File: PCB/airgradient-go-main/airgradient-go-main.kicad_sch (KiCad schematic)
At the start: 205 parts, among them CN1 HCZZ0032-5, CN2 HCZZ0032-5, CN3 HCZZ0032-5, Q1 SIA445EDJ-T1-GE3, Q2 ZVN4106FTA_C508255, Q3 CSD83325L, Q4 SS8050-G, Q5 SI1308EDL, SW1 TS-1091C-A1B3-D2, SW2 TS-1091C-A1B3-D2, U1 W25N512GVEIG, U10 SGP41-D-R4, U11 PS1-CO-SMOKE-10k, U12 SHT4x, U13 SPL07-003, U14 LIS2DH12TR, U15 TMUX121NKGR_C22428404, U16 S12, U17 TCA6408ARGT, U18 TAU1113, U19 LM66200DRLR, U2 ZDSD512MLGEAG, U20 LP5036, U3 BQ27742YZFR-G1, U4 ESP32-C5-MINI-1, U5 BQ25628RYKR, U6 HYG-8503A, U7 TPL5010DDCR, U8 TPS63802DLAR, U9 TPS7A0228DQNR, Y1 32.768kHz CL6pF

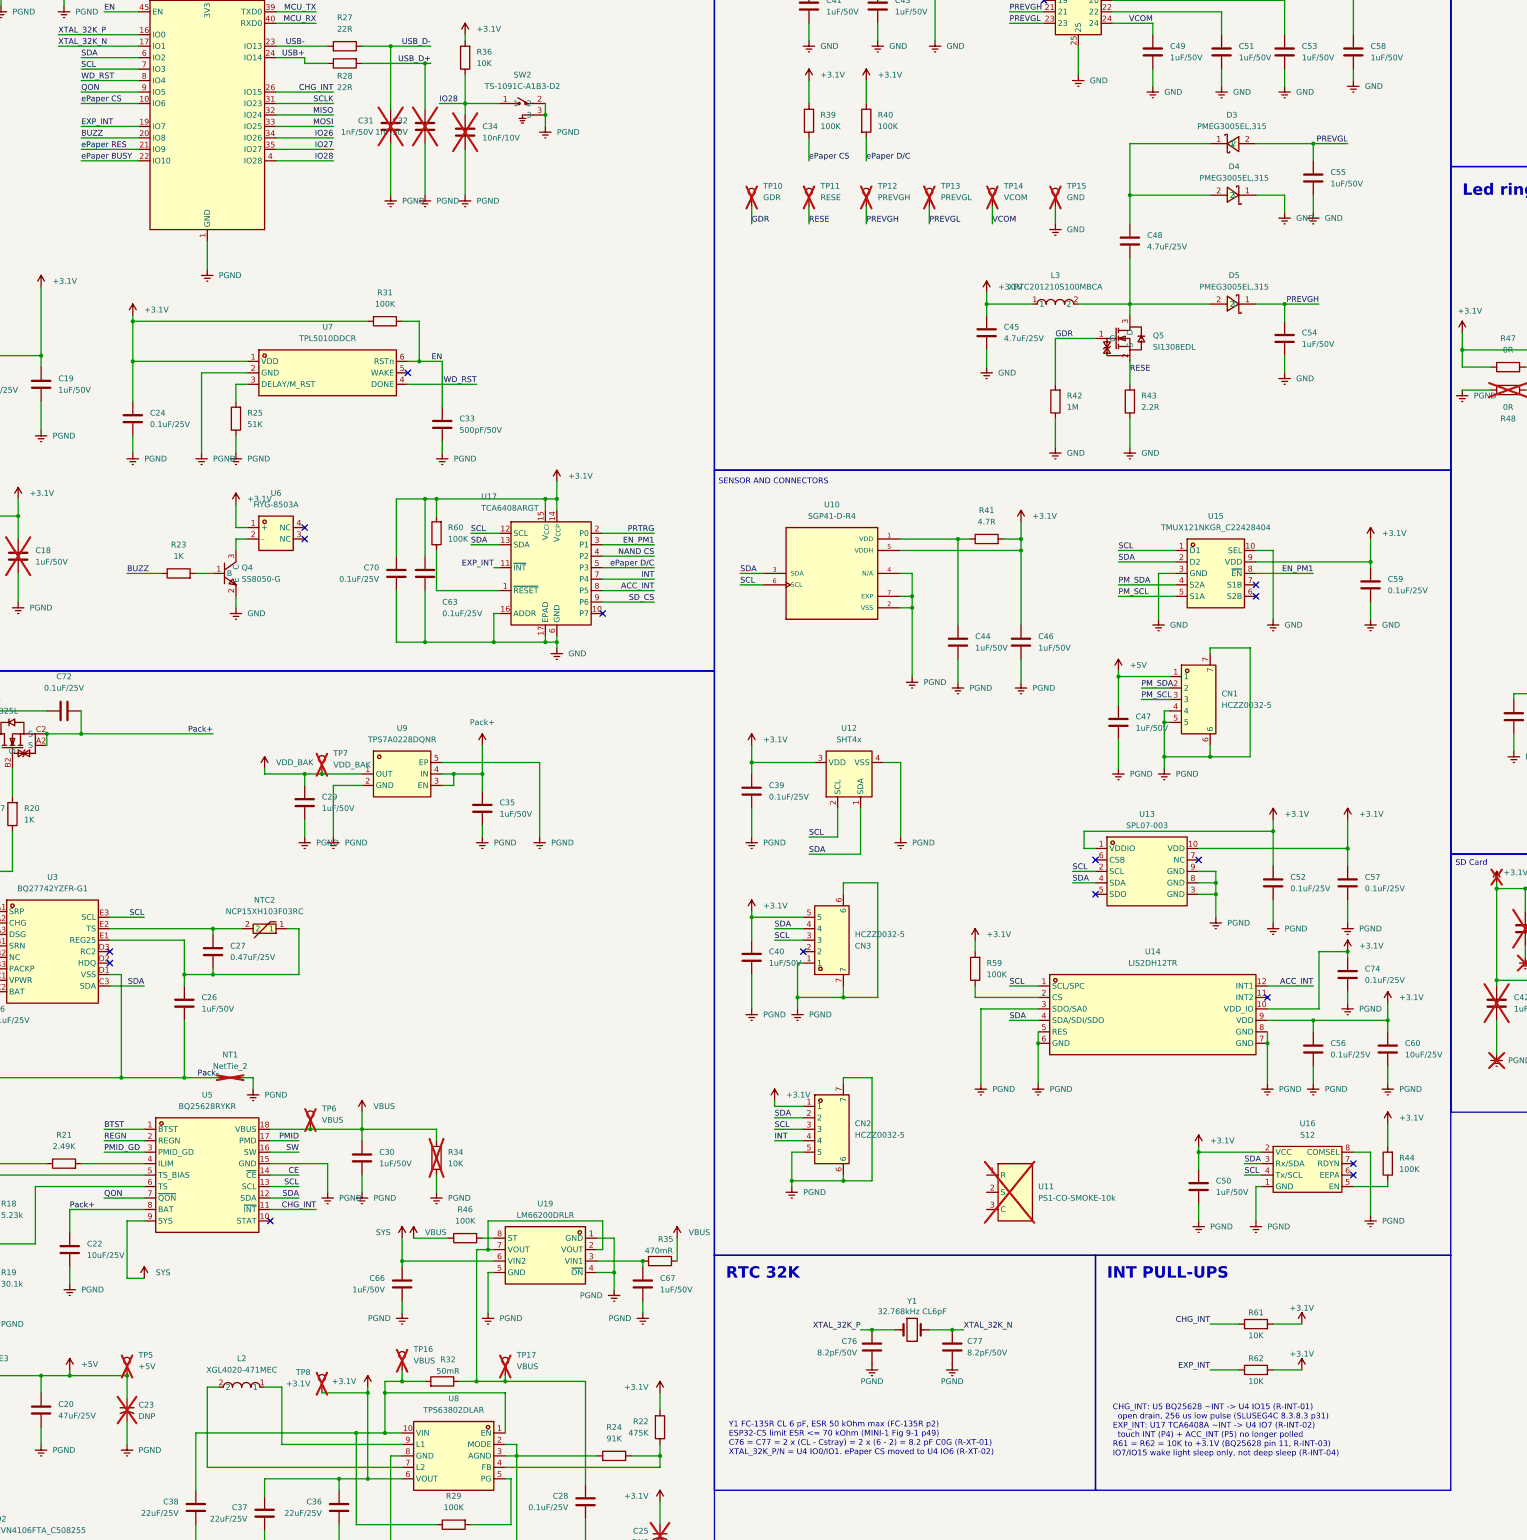
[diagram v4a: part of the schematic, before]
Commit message: Wire-OR the charger and expander INT onto IO7
At layout, U5 pin 11, U17 pin 11 and the IO15 pad turned out to be
walled in by existing routing (SDA escape via and SYS pour at U5,
SCL/SD_CS at U17, UART/NAND CS/MOSI at IO15). Both INT outputs are
open drain, so they now share one net, I2C_INT, into U4 IO7 with a
single 10K pull-up (R61); R62 is gone and IO15 is free again.

Firmware reads the TCA6408A input port and Charger_Flag_X on every
falling edge; the charger flags latch, so a pulse that arrives while
the expander holds the line low is not lost (R-INT-01..04).

lint: no new findings; ERC 269 -> 268 vs 1d977c7; net_diff 0 errors.
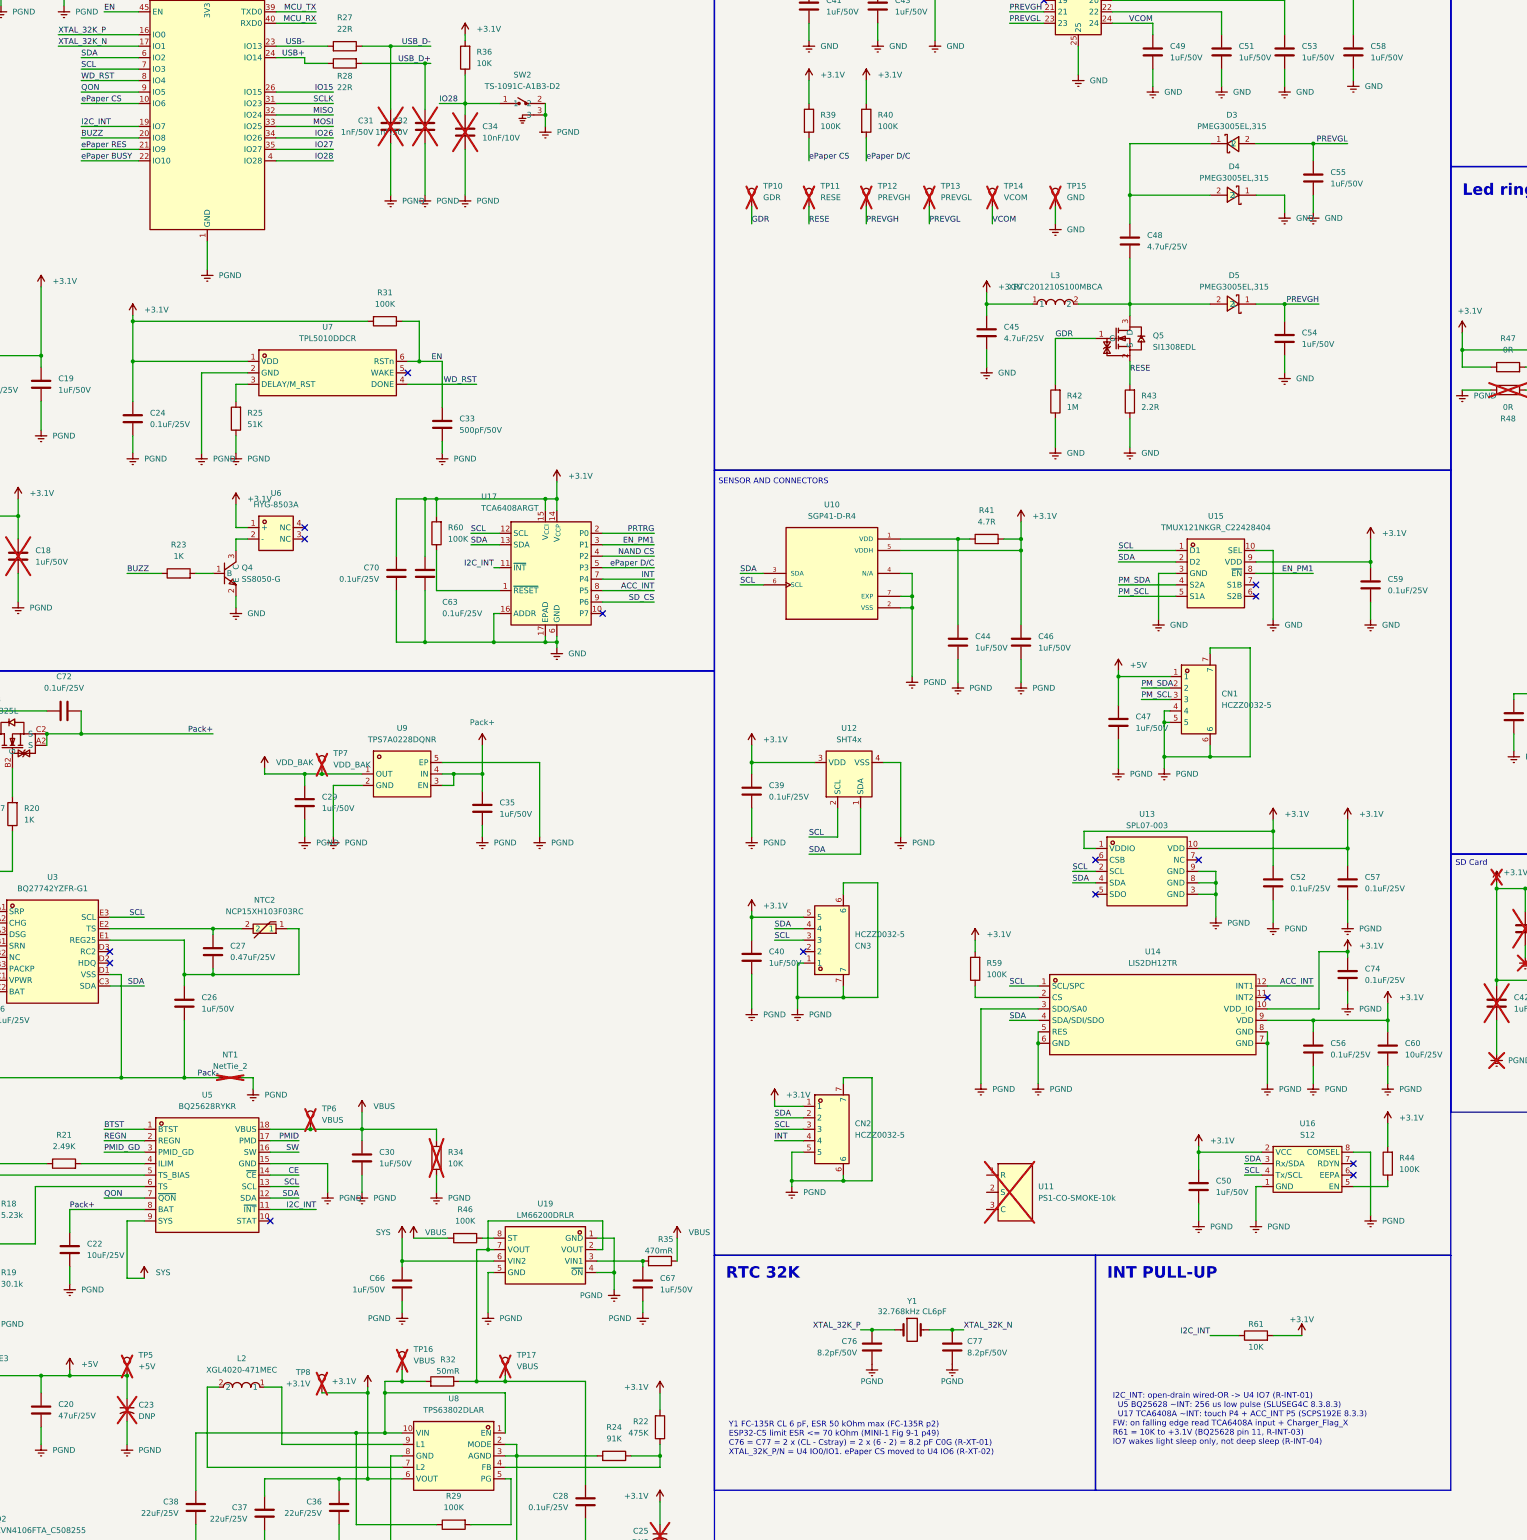
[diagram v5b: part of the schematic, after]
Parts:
- removed R62: 10K, Resistor_SMD:R_0402_1005Metric, symbol Device:R
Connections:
- net EXP_INT is gone; now on net I2C_INT: U17.11 (~{INT}), U4.19 (IO7)
- net CHG_INT renamed I2C_INT
- net I2C_INT: no longer U4.26 (IO15)
- new net IO15: U4.26 (IO15)
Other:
- note added: "I2C_INT: open-drain wired-OR -> U4 IO7 (R-INT-01) U5 BQ25628 ~INT: 256 us low pulse (SLUSEG4C 8.3.8.3) U17 TCA6408A ~INT: touch P4 + ACC_INT P5 (SCPS192E 8.3.3) FW: on falling edge read TCA6408A input + Charger_Flag_X R61 = 10K to +3.1V (BQ25628 pin 11, R-INT-03) IO7 wakes light sleep only, not deep sleep (R-INT-04)"
- note added: "INT PULL-UP"
- note removed: "CHG_INT: U5 BQ25628 ~INT -> U4 IO15 (R-INT-01) open drain, 256 us low pulse (SLUSEG4C 8.3.8.3 p31) EXP_INT: U17 TCA6408A ~INT -> U4 IO7 (R-INT-02) touch INT (P4) + ACC_INT (P5) no longer polled R61 = R62 = 10K to +3.1V (BQ25628 pin 11, R-INT-03) IO7/IO15 wake light sleep only, not deep sleep (R-INT-04)"
- note removed: "INT PULL-UPS"
- moved on the sheet: R61
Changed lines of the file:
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@@
 		)
 	)
-	(label "CHG_INT"
+	(label "I2C_INT"
 		(at 172.72 323.85 180)
 		(effects
@@
 		)
 	)
-	(label "EXP_INT"
+	(label "I2C_INT"
 		(at 212.09 181.61 180)
 		(effects
@@
 		)
 	)
-	(label "EXP_INT"
+	(label "I2C_INT"
 		(at 120.65 83.82 0)
 		(effects
@@
 		)
 	)
-	(label "CHG_INT"
+	(label "IO15"
 		(at 176.53 76.2 180)
 		(effects
@@
 	(wire
 		(pts
-			(xy 377.19 349.25) (xy 370.84 349.25)
+			(xy 377.19 351.79) (xy 370.84 351.79)
 		)
 		(stroke
@@
 		)
 	)
-	(label "CHG_INT"
-		(at 370.84 349.25 180)
+	(label "I2C_INT"
+		(at 370.84 351.79 180)
 		(effects
 			(font
@@
 	(wire
 		(pts
-			(xy 384.81 349.25) (xy 391.16 349.25)
-		)
-		(stroke
-			(width 0)
-			(type default)
-		)
-	)
-	(wire
-		(pts
-			(xy 377.19 359.41) (xy 370.84 359.41)
-		)
-		(stroke
-			(width 0)
-			(type default)
-		)
-	)
-	(label "EXP_INT"
-		(at 370.84 359.41 180)
-		(effects
-			(font
-				(size 1.27 1.27)
-			)
-			(justify right bottom)
-		)
-	)
-	(wire
-		(pts
-			(xy 384.81 359.41) (xy 391.16 359.41)
+			(xy 384.81 351.79) (xy 391.16 351.79)
 		)
 		(stroke
@@
 	(symbol
 		(lib_id "Device:R")
-		(at 381 349.25 90)
+		(at 381 351.79 90)
 		(unit 1)
 		(body_style 1)
@@
 		(fields_autoplaced yes)
 		(property "Reference" "R61"
-			(at 381 346.71 90)
+			(at 381 349.25 90)
 			(show_name no)
 			(do_not_autoplace no)
@@
 		)
 		(property "Value" "10K"
-			(at 381 351.79 90)
+			(at 381 354.33 90)
 			(show_name no)
 			(do_not_autoplace no)
@@
 		)
 		(property "Footprint" "Resistor_SMD:R_0402_1005Metric"
-			(at 381 349.25 0)
+			(at 381 351.79 0)
 			(hide yes)
 			(show_name no)
@@
 		)
 		(property "Datasheet" "https://lcsc.com/product-detail/Others_Huaxin-S-T-MR04X1002FTL_C327797.html"
-			(at 381 349.25 0)
+			(at 381 351.79 0)
 			(hide yes)
 			(show_name no)
@@
 		)
 		(property "Description" "MR04X1002FTL"
-			(at 381 349.25 0)
+			(at 381 351.79 0)
 			(hide yes)
 			(show_name no)
@@
 		)
 		(property "LCSC Part" "C327797"
-			(at 381 349.25 0)
+			(at 381 351.79 0)
 			(hide yes)
 			(show_name no)
@@
 	)
 	(symbol
-		(lib_id "Device:R")
-		(at 381 359.41 90)
-		(unit 1)
-		(body_style 1)
-		(exclude_from_sim no)
-		(in_bom yes)
-		(on_board yes)
-		(in_pos_files yes)
-		(dnp no)
-		(fields_autoplaced yes)
-		(property "Reference" "R62"
-			(at 381 356.87 90)
-			(show_name no)
-			(do_not_autoplace no)
-			(effects
-				(font
-					(size 1.27 1.27)
-				)
-			)
-		)
-		(property "Value" "10K"
-			(at 381 361.95 90)
-			(show_name no)
-			(do_not_autoplace no)
-			(effects
-				(font
-					(size 1.27 1.27)
-				)
-			)
-		)
-		(property "Footprint" "Resistor_SMD:R_0402_1005Metric"
-			(at 381 359.41 0)
-			(hide yes)
-			(show_name no)
-			(do_not_autoplace no)
-			(effects
-				(font
-					(size 1.27 1.27)
-				)
-			)
-		)
-		(property "Datasheet" "https://lcsc.com/product-detail/Others_Huaxin-S-T-MR04X1002FTL_C327797.html"
-			(at 381 359.41 0)
-			(hide yes)
-			(show_name no)
-			(do_not_autoplace no)
-			(effects
-				(font
-					(size 1.27 1.27)
-				)
-			)
-		)
-		(property "Description" "MR04X1002FTL"
-			(at 381 359.41 0)
-			(hide yes)
-			(show_name no)
-			(do_not_autoplace no)
-			(effects
-				(font
-					(size 1.27 1.27)
-				)
-			)
-		)
-		(property "LCSC Part" "C327797"
-			(at 381 359.41 0)
-			(hide yes)
-			(show_name no)
-			(do_not_autoplace no)
-			(effects
-				(font
-					(size 1.27 1.27)
-				)
-			)
-		)
-		(pin "1"
-		)
-		(pin "2"
-		)
-		(instances
-			(project "airgradient-go-main"
-				(path "/63bfc1c7-4623-455a-8f83-dca1d491c7db"
-					(reference "R62")
-					(unit 1)
-				)
-			)
-		)
-	)
-	(symbol
 		(lib_id "power:VDD")
-		(at 391.16 349.25 0)
+		(at 391.16 351.79 0)
 		(unit 1)
 		(body_style 1)
@@
 		(fields_autoplaced yes)
 		(property "Reference" "#PWR003"
-			(at 391.16 353.06 0)
+			(at 391.16 355.6 0)
 			(hide yes)
 			(show_name no)
@@
 		)
 		(property "Value" "+3.1V"
-			(at 391.16 345.694 0)
+			(at 391.16 348.234 0)
 			(show_name no)
 			(do_not_autoplace no)
@@
 		)
 		(property "Footprint" ""
-			(at 391.16 349.25 0)
+			(at 391.16 351.79 0)
 			(hide yes)
 			(show_name no)
@@
 		)
 		(property "Datasheet" ""
-			(at 391.16 349.25 0)
+			(at 391.16 351.79 0)
 			(hide yes)
 			(show_name no)
@@
 		)
 		(property "Description" "Power symbol creates a global label with name \"VDD\""
-			(at 391.16 349.25 0)
+			(at 391.16 351.79 0)
 			(hide yes)
 			(show_name no)
@@
 		)
 	)
-	(symbol
-		(lib_id "power:VDD")
-		(at 391.16 359.41 0)
-		(unit 1)
-		(body_style 1)
-		(exclude_from_sim no)
-		(in_bom yes)
-		(on_board yes)
-		(in_pos_files yes)
-		(dnp no)
-		(fields_autoplaced yes)
-		(property "Reference" "#PWR004"
-			(at 391.16 363.22 0)
-			(hide yes)
-			(show_name no)
-			(do_not_autoplace no)
-			(effects
-				(font
-					(size 1.27 1.27)
-				)
-			)
-		)
-		(property "Value" "+3.1V"
-			(at 391.16 355.854 0)
-			(show_name no)
-			(do_not_autoplace no)
-			(effects
-				(font
-					(size 1.27 1.27)
-				)
-			)
-		)
-		(property "Footprint" ""
-			(at 391.16 359.41 0)
-			(hide yes)
-			(show_name no)
-			(do_not_autoplace no)
-			(effects
-				(font
-					(size 1.27 1.27)
-				)
-			)
-		)
-		(property "Datasheet" ""
-			(at 391.16 359.41 0)
-			(hide yes)
-			(show_name no)
-			(do_not_autoplace no)
-			(effects
-				(font
-					(size 1.27 1.27)
-				)
-			)
-		)
-		(property "Description" "Power symbol creates a global label with name \"VDD\""
-			(at 391.16 359.41 0)
-			(hide yes)
-			(show_name no)
-			(do_not_autoplace no)
-			(effects
-				(font
-					(size 1.27 1.27)
-				)
-			)
-		)
-		(pin "1"
-		)
-		(instances
-			(project "airgradient-go-main"
-				(path "/63bfc1c7-4623-455a-8f83-dca1d491c7db"
-					(reference "#PWR004")
-					(unit 1)
-				)
-			)
-		)
-	)
 	(rectangle
 		(start 345.44 334.01)
@@
 		)
 	)
-	(text "INT PULL-UPS"
+	(text "INT PULL-UP"
 		(exclude_from_sim no)
 		(at 347.98 336.55 0)
@@
 		)
 	)
-	(text "CHG_INT: U5 BQ25628 ~INT -> U4 IO15 (R-INT-01)\n  open drain, 256 us low pulse (SLUSEG4C 8.3.8.3 p31)\nEXP_INT: U17 TCA6408A ~INT -> U4 IO7 (R-INT-02)\n  touch INT (P4) + ACC_INT (P5) no longer polled\nR61 = R62 = 10K to +3.1V (BQ25628 pin 11, R-INT-03)\nIO7/IO15 wake light sleep only, not deep sleep (R-INT-04)"
+	(text "I2C_INT: open-drain wired-OR -> U4 IO7 (R-INT-01)\n  U5 BQ25628 ~INT: 256 us low pulse (SLUSEG4C 8.3.8.3)\n  U17 TCA6408A ~INT: touch P4 + ACC_INT P5 (SCPS192E 8.3.3)\nFW: on falling edge read TCA6408A input + Charger_Flag_X\nR61 = 10K to +3.1V (BQ25628 pin 11, R-INT-03)\nIO7 wakes light sleep only, not deep sleep (R-INT-04)"
 		(exclude_from_sim no)
-		(at 349.25 367.03 0)
+		(at 349.25 364.49 0)
 		(effects
 			(font
